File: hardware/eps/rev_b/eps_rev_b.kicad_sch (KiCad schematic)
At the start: 0 parts

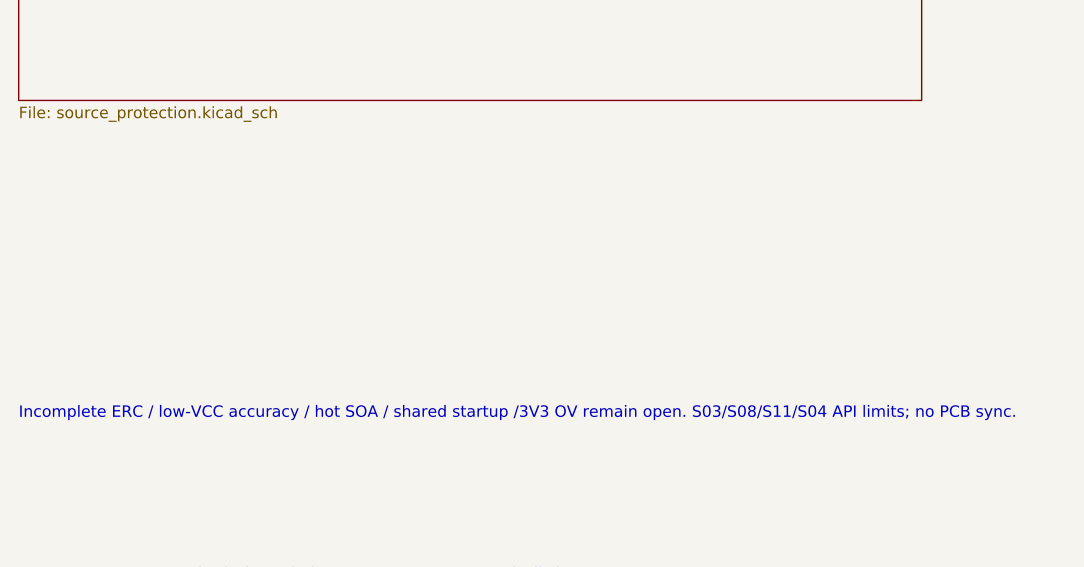
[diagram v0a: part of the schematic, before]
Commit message: Integrate supply-qualified SWD and reconcile EMBER stack geometry
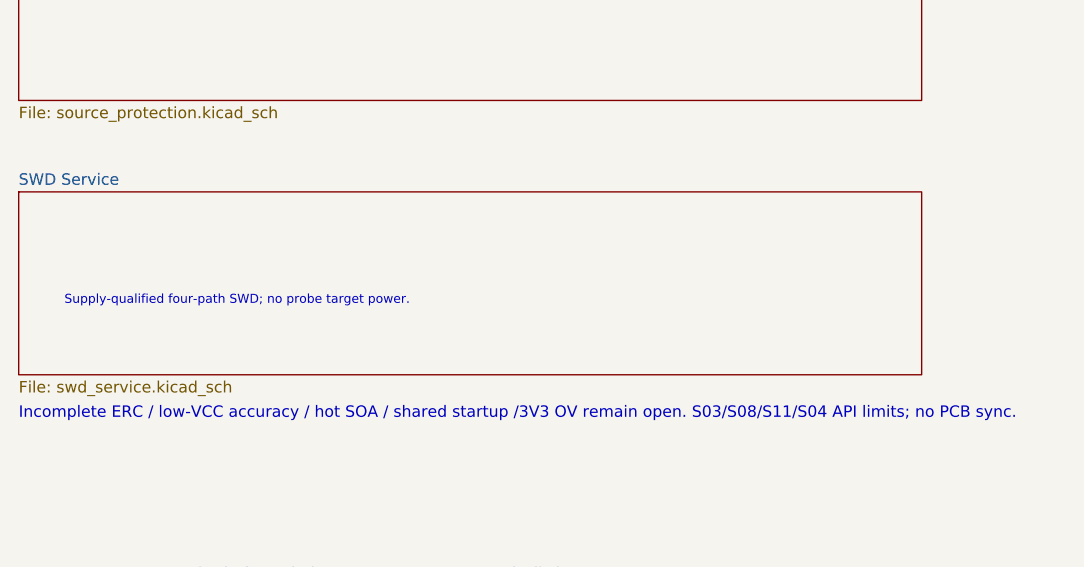
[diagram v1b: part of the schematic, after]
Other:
- added sheet SWD Service (swd_service.kicad_sch)
- note added: "Supply-qualified four-path SWD; no probe target power."
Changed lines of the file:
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@@
     (effects (font (size 0.85 0.85)) (justify left top))
   )
+	(sheet
+    (at 30.48 200.66)
+    (size 100.33 20.32)
+    (fields_autoplaced yes)
+    (stroke (width 0.1524) (type solid))
+    (fill (color 0 0 0 0.0))
+    (property "Sheetname" "SWD Service"
+      (at 30.48 200.025 0)
+      (effects (font (size 1.27 1.27)) (justify left bottom))
+    )
+    (property "Sheetfile" "swd_service.kicad_sch"
+      (at 30.48 221.61499999999998 0)
+      (effects (font (size 1.27 1.27)) (justify left top))
+    )
+    (instances
+      (project "eps_rev_b"
+        (path "/8eba9f22-6f11-42d7-8e4a-b8de8905b113" (page "13"))
+      )
+    )
+  )
+  (text "Supply-qualified four-path SWD; no probe target power."
+    (at 35.56 213.36 0)
+    (effects (font (size 1 1)) (justify left bottom))
+  )
 )

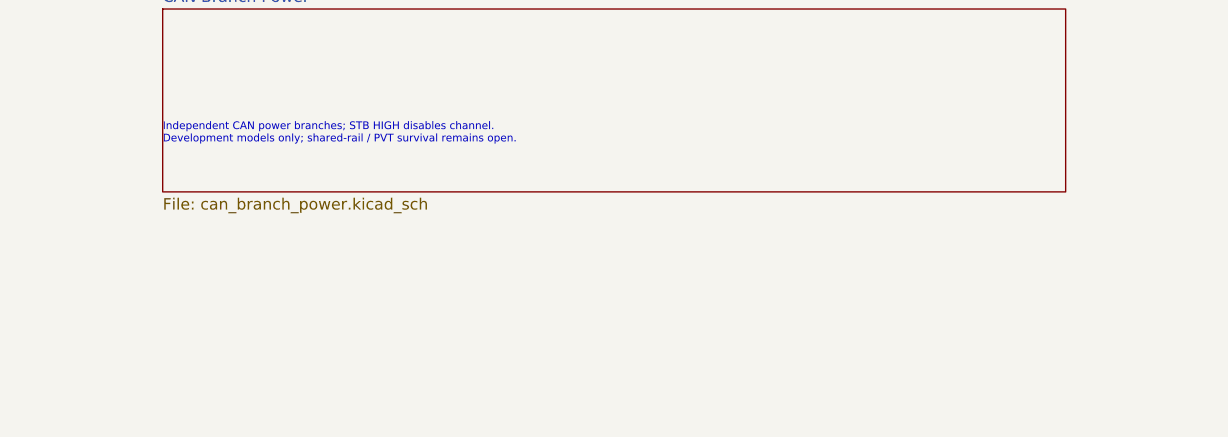
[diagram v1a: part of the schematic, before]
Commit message: Integrate EPS rail telemetry and record source-guard limits
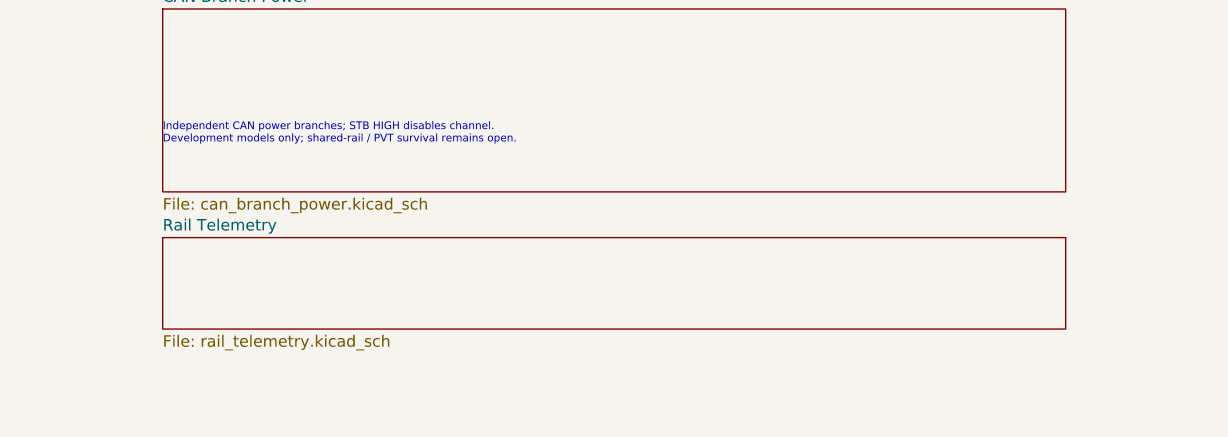
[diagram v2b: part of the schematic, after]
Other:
- added sheet Rail Telemetry (rail_telemetry.kicad_sch)
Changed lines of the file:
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@@
     (effects (font (size 1 1)) (justify left bottom))
   )
+	(sheet
+    (at 167.64 226.06)
+    (size 100.33 10.16)
+    (fields_autoplaced yes)
+    (stroke (width 0.1524) (type solid))
+    (fill (color 0 0 0 0.0))
+    (property "Sheetname" "Rail Telemetry"
+      (at 167.64 225.425 0)
+      (effects (font (size 1.27 1.27)) (justify left bottom))
+    )
+    (property "Sheetfile" "rail_telemetry.kicad_sch"
+      (at 167.64 236.855 0)
+      (effects (font (size 1.27 1.27)) (justify left top))
+    )
+    (instances
+      (project "eps_rev_b"
+        (path "/8eba9f22-6f11-42d7-8e4a-b8de8905b113" (page "14"))
+      )
+    )
+  )
 )
